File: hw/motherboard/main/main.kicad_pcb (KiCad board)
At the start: 4 copper layers, 100 x 100 mm, 131 parts, among them J1 SWD holes, J10 stack[0..3], J11 stack[0..3], J12 stack[0..3], J13 GPIO, J2 Conn_ARM_JTAG_SWD_10, J3 690-005-299-043, J4 STACK_GND, J5 RGB stack, J6 5V power in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

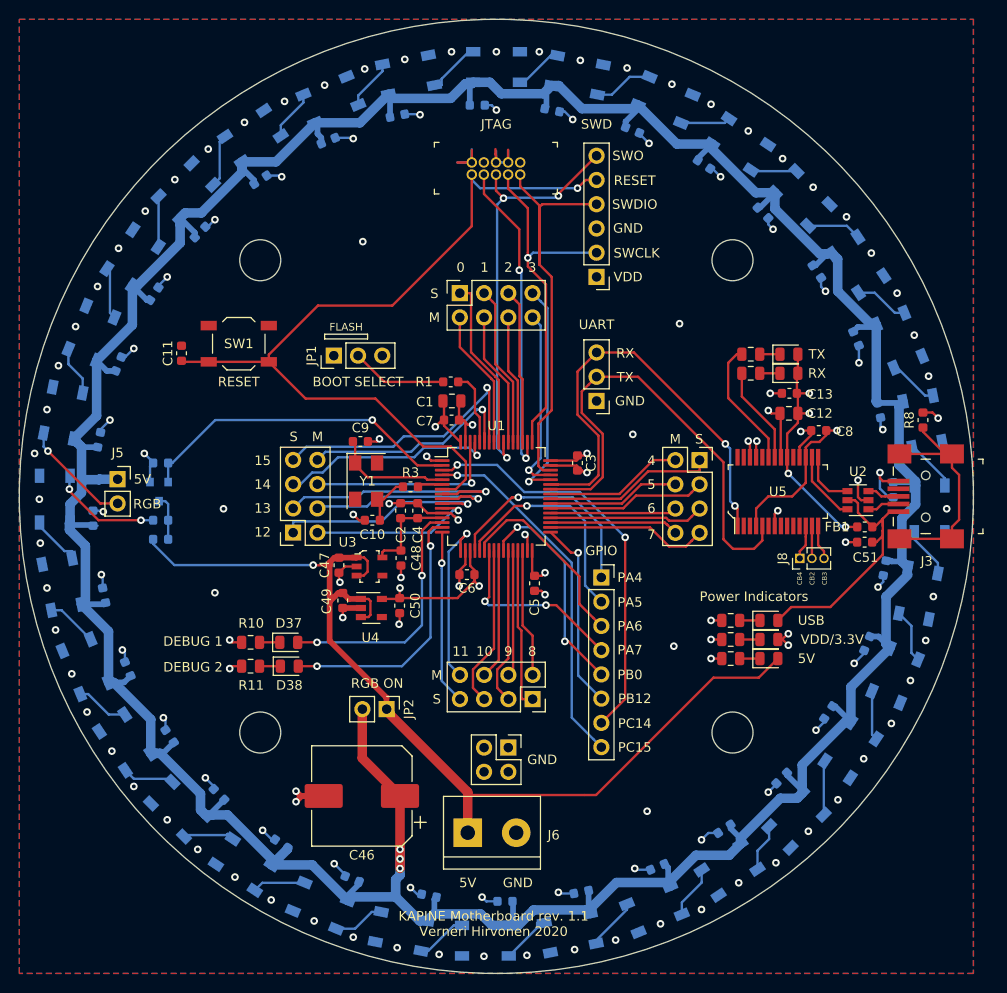
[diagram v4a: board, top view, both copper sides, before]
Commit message: Add reverse polarity protection to +5V input. Bump revision number to 1.2.
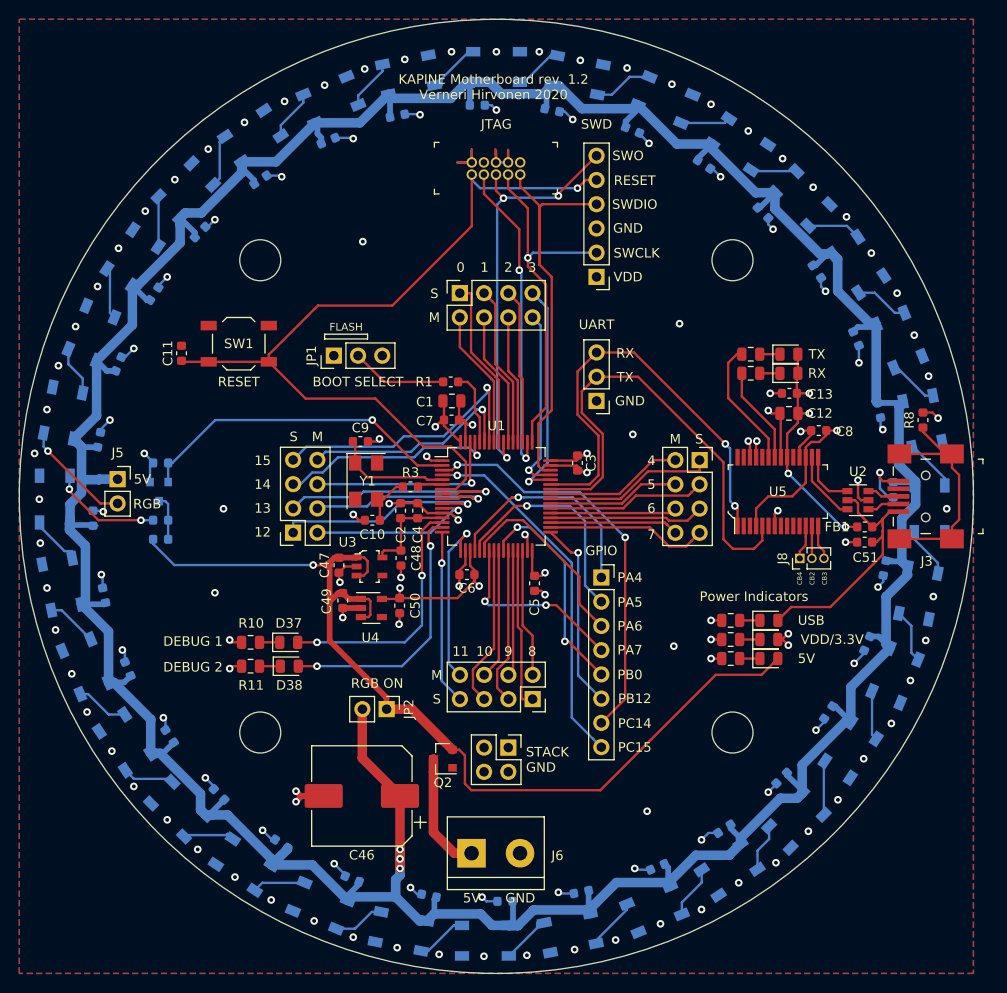
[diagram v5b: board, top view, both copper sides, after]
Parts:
- added Q2: Q_PMOS_GSD, Package_TO_SOT_SMD:SOT-23, F.Cu at (144.4, 127.5)
- C10, C9: value 20p -> 27p
- R10, R11: value 1K -> 1k
- R6, R7: value TBD -> 1k
- moved J6 2.19 mm to (147.4, 137.4)
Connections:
- J6 pad 1: +5V -> Net-(J6-Pad1)
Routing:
- net Net-(J6-Pad1): track 0.00 -> 12.6 mm
- net +5V: track 107.1 -> 104.3 mm
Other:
- board text added: "KAPINE Motherboard rev. 1.2 Verneri Hirvonen 2020"
- board text added: "STACK GND"
- board text removed: "KAPINE Motherboard rev. 1.1 Verneri Hirvonen 2020"
